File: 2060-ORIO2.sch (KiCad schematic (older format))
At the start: 195 parts, among them J11 RaspberryPI-B+header, J12 Conn_01x04, J13 Conn_01x08, J14 Conn_01x02, J15 Conn_01x08, J16 Conn_01x10, J17 Conn_01x10, J18 Conn_01x10, J19 Conn_01x10, J20 Conn_01x09, J21 Conn_01x08, J22 Conn_01x08, J23 Conn_01x08, J24 Conn_01x08, J25 Conn_01x08, J26 Conn_01x08, J27 Conn_01x02, J28 Conn_01x16, J29 Conn_01x16, J30 Conn_01x16, J31 Conn_01x08, J32 Conn_01x08, J33 Conn_01x08, J34 Conn_01x08, J35 TBL001-500-02GY-2GY, Q11 ULN2803ADWR, Q12 BCV27, SW11 SW_DIP_x08, U11 ICE40HX4K-TQ144, U12 SN74LVC4245AN, U13 SN74LVC4245AN, U14 SN74LVC4245AN, U15 TPS563231, U16 MCP3008, U17 AZ1117CH-3.3TRG1, U18 AZ1117CH-3.3TRG1, U19 AZ1117CH-1.2, U20 TPS563231, U21 SN74LVC4245AN, U22 SN74LVC4245AN, U23 SN74LVC4245AN, U24 SN74LVC4245AN, U25 TPS563231, U26 AP3012, Y11 XLH536025_000000I

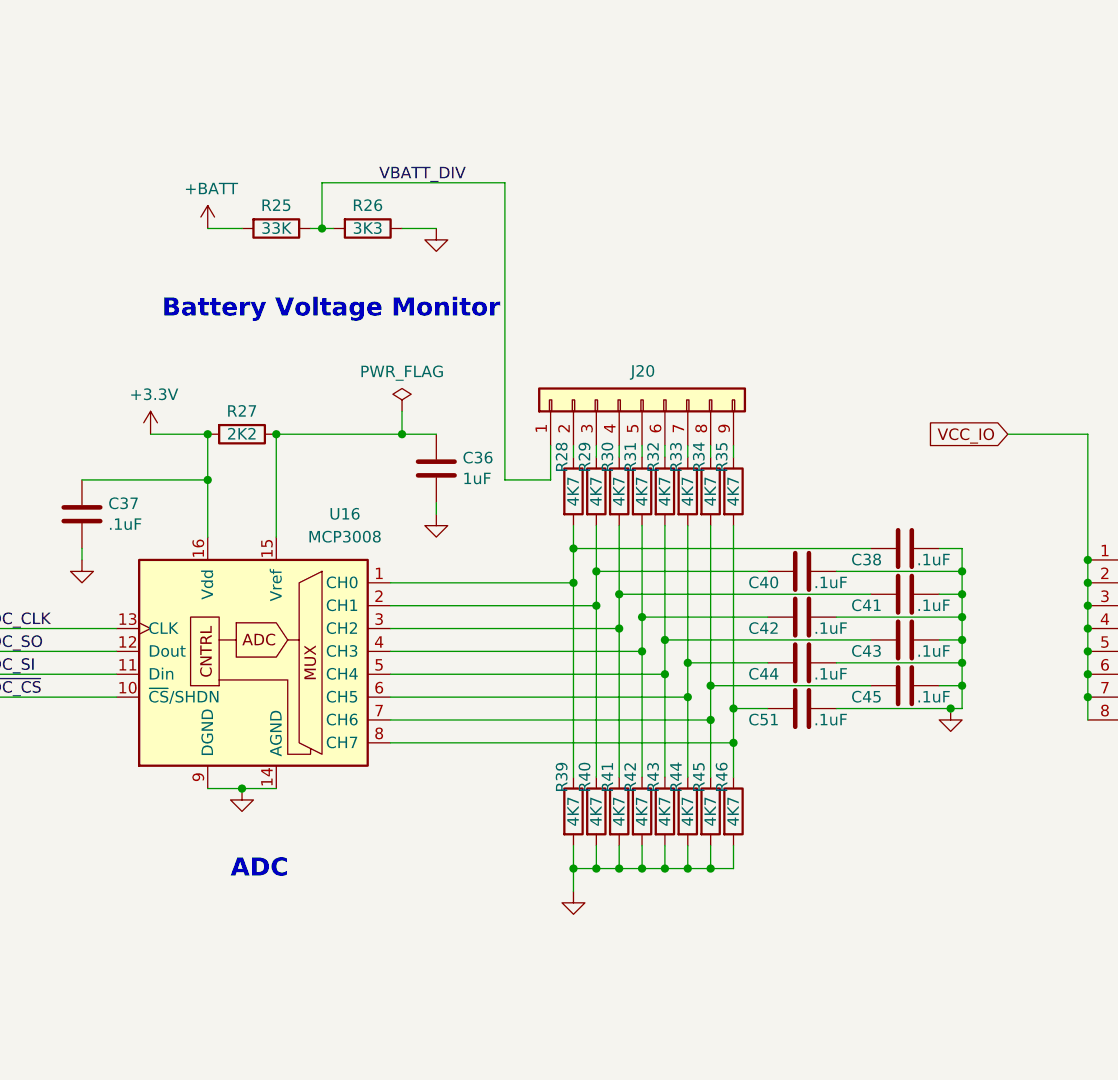
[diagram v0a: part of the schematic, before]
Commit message: Change ADC ref voltage resistor to 100 ohms.
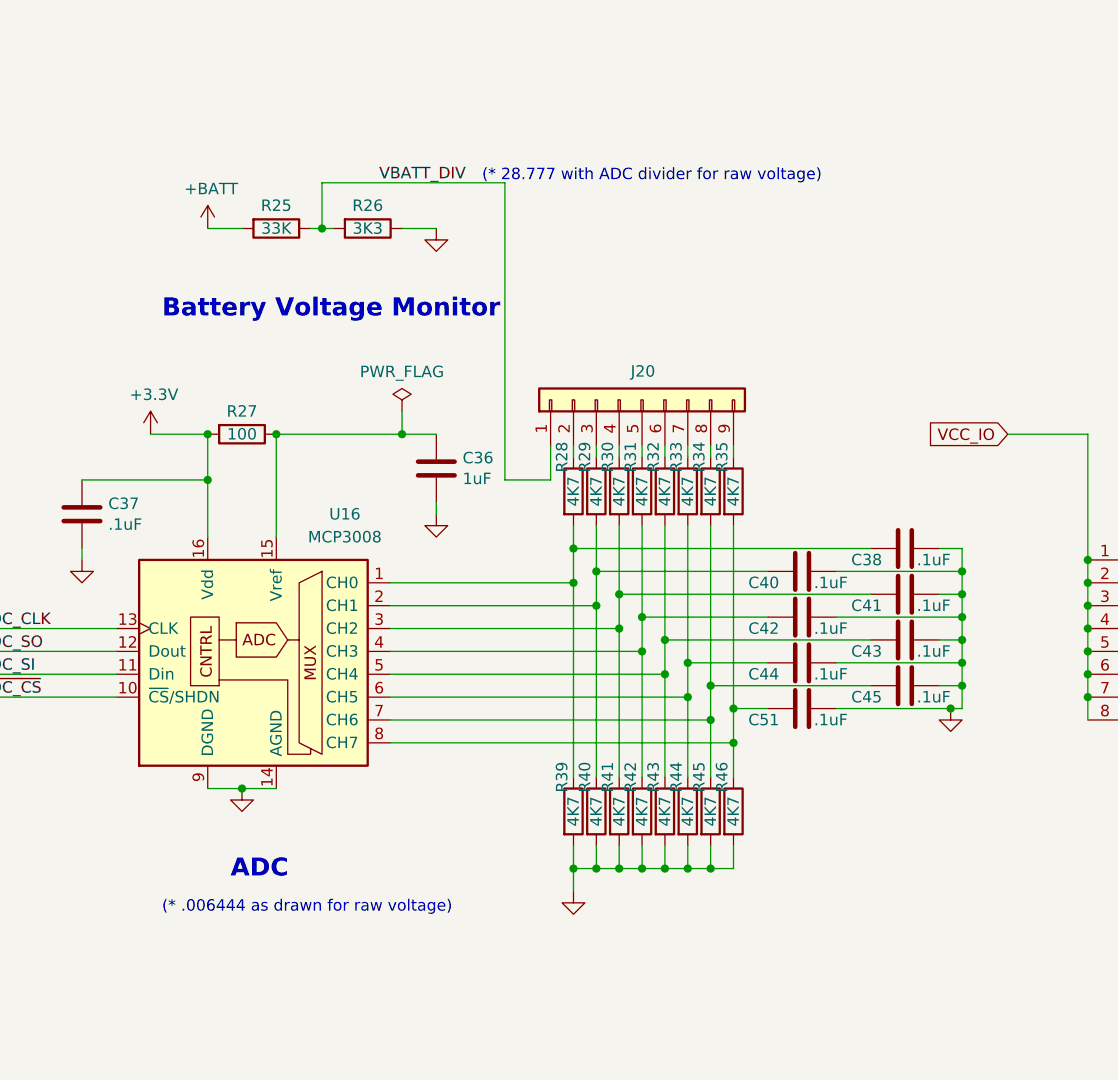
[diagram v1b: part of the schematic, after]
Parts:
- R27: value 2K2 -> 100; Description RES SMD 2.2K OHM 1% 1/10W 0603 -> RES SMD 100 OHM 1% 1/10W 0603; Digi-Key_PN 311-2.20KHRCT-ND -> 311-100HRCT-ND; MPN RC0603FR-072K2L -> RC0603FR-07100RL
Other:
- note added: "(* .006444 as drawn for raw voltage)"
- note added: "(* 28.777 with ADC divider for raw voltage)"
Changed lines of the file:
@@
 AR Path="/5ECC13DB/63C02E3E" Ref="R?"  Part="1"
 F 0 "R27" V 16450 8650 50  0000 C CNN
-F 1 "2K2" V 16550 8650 50  0000 C CNN
+F 1 "100" V 16550 8650 50  0000 C CNN
 F 2 "Resistor_SMD:R_0603_1608Metric_Pad1.05x0.95mm_HandSolder" V 16480 8650 50  0001 C CNN
 F 3 "~" H 16550 8650 50  0001 C CNN
-F 4 "311-2.20KHRCT-ND" H 16550 8650 50  0001 C CNN "Digi-Key_PN"
-F 5 "RES SMD 2.2K OHM 1% 1/10W 0603" H 16550 8650 50  0001 C CNN "Description"
-F 6 "RC0603FR-072K2L" H 16550 8650 50  0001 C CNN "MPN"
+F 4 "311-100HRCT-ND" H 16550 8650 50  0001 C CNN "Digi-Key_PN"
+F 5 "RES SMD 100 OHM 1% 1/10W 0603" H 16550 8650 50  0001 C CNN "Description"
+F 6 "RC0603FR-07100RL" H 16550 8650 50  0001 C CNN "MPN"
 F 7 "Yageo" H 16550 8650 50  0001 C CNN "Manufacturer"
 	1    16550 8650
@@
 	0    1    -1   0
 $EndComp
+Text Notes 17600 7550 0    50   ~ 0
+(* 28.777 with ADC divider for raw voltage)
+Text Notes 16200 10750 0    50   ~ 0
+(* .006444 as drawn for raw voltage)
 $EndSCHEMATC

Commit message: Change regulators & add current limiters.
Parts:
- removed C31, C33, C35, C60, C62, C69, C71: .1uF, Capacitor_SMD:C_0603_1608Metric_Pad1.05x0.95mm_HandSolder, symbol Device:C
- removed F11: .5A, Fuse:Fuse_2920_7451Metric_Pad2.10x5.45mm_HandSolder, symbol Device:Polyfuse
- removed J27: Conn_01x02, Connector_PinHeader_2.54mm:PinHeader_1x02_P2.54mm_Vertical, symbol Connector_Generic:Conn_01x02
- removed R12, R13, R15, R16, R17, R18, R19: 33, Resistor_SMD:R_0603_1608Metric_Pad1.05x0.95mm_HandSolder, symbol Device:R
- removed U12, U13, U14, U21, U22, U23, U24: SN74LVC4245AN, Package_SO:TSSOP-24_4.4x7.8mm_P0.65mm, symbol jb-symbol:SN74LVC4245AN
- removed U15, U20, U25: TPS563231, jb-footprint:SOT-563, symbol JWlib:TPS563231
- added C80, C81, C84, C85: 22uF, Capacitor_SMD:C_0805_2012Metric_Pad1.15x1.40mm_HandSolder, symbol Device:C
- added C82, C83: .001uF, Capacitor_SMD:C_0603_1608Metric_Pad1.05x0.95mm_HandSolder, symbol Device:C
- added Q91, Q92, Q93, Q94: BCV27, Package_TO_SOT_SMD:SOT-23, symbol Device:Q_NPN_Darlington_BEC
- added R55, R56, R57: x, Resistor_SMD:R_0603_1608Metric_Pad1.05x0.95mm_HandSolder, symbol Device:R
- added R91, R93: 10K, Resistor_SMD:R_0603_1608Metric_Pad1.05x0.95mm_HandSolder, symbol Device:R
- added R92, R94: 1.2, Resistor_SMD:R_1210_3225Metric_Pad1.42x2.65mm_HandSolder, symbol Device:R
- added RN14: 33, Resistor_SMD:R_Array_Convex_8x0602, symbol Device:R_Pack08
- added SW1: SW_DIP_x01, Button_Switch_THT:SW_DIP_SPSTx01_Slide_6.7x4.1mm_W7.62mm_P2.54mm_LowProfile, symbol Switch:SW_DIP_x01
- added U1, U15, U20: AOZ2151TQI-19, jb-footprint:AOZ2151TQI-19, symbol jb-symbol:AOZ2151TQI-19
- added U12, U13, U14, U21, U22, U23, U24: ‎74LVT245B, Package_SO:TSSOP-20_4.4x6.5mm_P0.65mm, symbol jb-symbol:‎74LVT245B
- C46, C67: value .1uF -> 4.7uF; Description CAP CER 0.1UF 25V X5R 0603 -> (none); Digi-Key_PN 445-6854-1-ND -> (none); MPN C1608X5R1E104K -> (none); Manufacturer TDK Corporation -> (none)
- C47: value 10uF -> 22uF; Description CAP CER 10UF 25V X5R 0805 -> (none); Digi-Key_PN 587-2985-1-ND -> (none); MPN TMK212BBJ106KG-T -> (none); Manufacturer Taiyo Yuden -> (none)
- C50, C58: value .1uF -> 22uF; footprint Capacitor_SMD:C_0603_1608Metric_Pad1.05x0.95mm_HandSolder -> Capacitor_SMD:C_0805_2012Metric_Pad1.15x1.40mm_HandSolder; Description CAP CER 0.1UF 25V X5R 0603 -> CAP CER 22UF 10V X5R 0805; Digi-Key_PN 445-6854-1-ND -> 490-10746-1-ND; MPN C1608X5R1E104K -> GRM21BR61A226ME44L; Manufacturer TDK Corporation -> Murata Electronics
- C63, C77: value .1uF -> 22uF; footprint Capacitor_SMD:C_0603_1608Metric_Pad1.05x0.95mm_HandSolder -> Capacitor_SMD:C_0805_2012Metric_Pad1.15x1.40mm_HandSolder; Description CAP CER 0.1UF 25V X5R 0603 -> (none); Digi-Key_PN 445-6854-1-ND -> (none); MPN C1608X5R1E104K -> (none); Manufacturer TDK Corporation -> (none)
- C64: value 10uF -> .1uF; footprint Capacitor_SMD:C_0805_2012Metric_Pad1.15x1.40mm_HandSolder -> Capacitor_SMD:C_0603_1608Metric_Pad1.05x0.95mm_HandSolder; Description CAP CER 10UF 25V X5R 0805 -> CAP CER 0.1UF 25V X5R 0603; Digi-Key_PN 587-2985-1-ND -> 445-6854-1-ND; MPN TMK212BBJ106KG-T -> C1608X5R1E104K; Manufacturer Taiyo Yuden -> TDK Corporation
- C73: value .1uF -> .001uF; Description CAP CER 0.1UF 25V X5R 0603 -> (none); Digi-Key_PN 445-6854-1-ND -> (none); MPN C1608X5R1E104K -> (none); Manufacturer TDK Corporation -> (none)
- C74: value 10uF -> 4.7uF; footprint Capacitor_SMD:C_0805_2012Metric_Pad1.15x1.40mm_HandSolder -> Capacitor_SMD:C_0603_1608Metric_Pad1.05x0.95mm_HandSolder; Description CAP CER 10UF 25V X5R 0805 -> (none); Digi-Key_PN 587-2985-1-ND -> (none); MPN TMK212BBJ106KG-T -> (none); Manufacturer Taiyo Yuden -> (none)
- L11, L12, L13: value 4.7uH -> 2.2uH; footprint Inductor_SMD:L_Bourns_SRN6045TA -> Inductor_SMD:L_Taiyo-Yuden_MD-4040; Description FIXED IND 4.7UH 4.5A 26 MOHM SMD -> (none); Digi-Key_PN SRN6045TA-4R7MCT-ND -> (none); MPN SRN6045TA-4R7M -> (none); Manufacturer Bourns Inc. -> (none)
- R36: value 45K3 -> x; Description RES 45.3K OHM 1% 1/10W 0603 -> (none); Digi-Key_PN RMCF0603FT45K3CT-ND -> (none); MPN RMCF0603FT45K3 -> (none); Manufacturer Stackpole Electronics Inc -> (none)
- R37, R48, R50: value 10K -> x; Description RES SMD 10K OHM 1% 1/10W 0603 -> (none); Digi-Key_PN 311-10.0KHRCT-ND -> (none); MPN RC0603FR-0710KL -> (none); Manufacturer Yageo -> (none)
- R38: value 16K2 -> x
- R47: value 73K2 -> x; Description RES SMD 73.2K OHM 1% 1/10W 0603 -> (none); Digi-Key_PN 311-73.2KHRCT-ND -> (none); MPN RC0603FR-0773K2L -> (none); Manufacturer Yageo -> (none)
- R49: value 90K -> x; Description RES 90.9K OHM 1% 1/10W 0603 -> (none); Digi-Key_PN RMCF0603FT90K9CT-ND -> (none); MPN RMCF0603FT90K9 -> (none); Manufacturer Stackpole Electronics Inc -> (none)
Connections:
- net labels added: VB_RSL, VB_RSOL
- net labels removed: VCC_SOL_12
- wire segments 1187 -> 1176
- no-connect marks 37 -> 42
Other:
- note added: ".5 Watt"
- note added: "24V @ 500mA Boost Regulator"
- note added: "500ma Current Limiter"
- note added: "5V Tolerant Quadrature Input"
- note added: "ON = 5V\nOFF = 3.3V"
- note added: "PWM output"
- note removed: "24V @ 500mA"
- note removed: "PWM w/output level shifter"
- note removed: "Quadrature VCC_IO input level shifter"
- note removed: "Shunt J35 for 5V.\nRemove for 3.3V."
- moved on the sheet: C16, C17, C18, C19, C20, C21, C22, C23, C24, C25, C26, C27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

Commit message: Change +BATT voltage divider to /6.
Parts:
- removed R26: 3K3, Resistor_SMD:R_0603_1608Metric_Pad1.05x0.95mm_HandSolder, symbol Device:R
- R25: value 33K -> 18K8
- R36: value x -> 3K4
- R37, R48, R50: value x -> 1K6
- R38: value x -> 5K
- R47: value x -> 8K4
- R49: value x -> 10K4
- R55, R56, R57: value x -> 0
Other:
- note added: "(* 6V with ADC divider for raw voltage)"
- note added: "ON = 3.3V\nOFF = 5V"
- note removed: "(* 28.777 with ADC divider for raw voltage)"
- note removed: "ON = 5V\nOFF = 3.3V"
- moved on the sheet: C47, R25, R36, R38, SW1

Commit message: Version 2.1 As ordered from JLCPCB.
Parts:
- C46, C67, C74: Description (none) -> CAP CER 4.7UF 10V X5R 0603; Digi-Key_PN (none) -> 1276-1044-1-ND; MPN (none) -> CL10A475KP8NNNC; Manufacturer (none) -> Samsung Electro-Mechanics
- C47, C63, C77: Description (none) -> CAP CER 22UF 25V X5R 0805; Digi-Key_PN (none) -> 490-14661-1-ND; MPN (none) -> GRM21BR61E226ME44K; Manufacturer (none) -> Murata Electronics
- C73, C82, C83: Description (none) -> CAP CER 1000PF 50V X7R 0603; Digi-Key_PN (none) -> 478-1215-1-ND; MPN (none) -> 06035C102KAT2A; Manufacturer (none) -> AVX Corporation
- H11, H12, H13, H14, H15, H16, H17, H18: Description (none) -> x; Digi-Key_PN (none) -> x; MPN (none) -> x
- J11, J12, J16, J17, J18, J19: Description (none) -> x; Digi-Key_PN (none) -> x; MPN (none) -> x; Manufacturer (none) -> x
- L11, L12, L13: Description (none) -> FIXED IND 2.2UH 4.3A 48 MOHM SMD; Digi-Key_PN (none) -> 553-3290-1-ND; MPN (none) -> PA4332.222NLT; Manufacturer (none) -> Pulse Electronics Power
- R25: Description RES SMD 33K OHM 1% 1/10W 0603 -> RES SMD 18K OHM 1% 1/10W 0603; Digi-Key_PN 311-33.0KHRCT-ND -> 311-18.0KHRCT-ND; MPN RC0603FR-0733KL -> RC0603FR-0718KL
- R36: Description (none) -> RES 3.4K OHM 1% 1/10W 0603; Digi-Key_PN (none) -> RMCF0603FT3K40CT-ND; MPN (none) -> RMCF0603FT3K40; Manufacturer (none) -> Stackpole Electronics Inc
- R37, R48, R50: Description (none) -> RES 1.6K OHM 1% 1/10W 0603; Digi-Key_PN (none) -> RMCF0603FT1K60CT-ND; MPN (none) -> RMCF0603FT1K60; Manufacturer (none) -> Stackpole Electronics Inc
- R38: Description RES 16.2K OHM 1% 1/10W 0603 -> RES SMD 5.1K OHM 1% 1/10W 0603; Digi-Key_PN RMCF0603FT16K2CT-ND -> CR0603-FX-5101ELFCT-ND; MPN RMCF0603FT16K2 -> CR0603-FX-5101ELF; Manufacturer Stackpole Electronics Inc -> Bourns Inc.
- R47: Description (none) -> RES 8.45K OHM 1% 1/10W 0603; Digi-Key_PN (none) -> RMCF0603FT8K45CT-ND; MPN (none) -> RMCF0603FT8K45; Manufacturer (none) -> Stackpole Electronics Inc
- R49: Description (none) -> RES 10.5K OHM 1% 1/10W 0603; Digi-Key_PN (none) -> RMCF0603FT10K5CT-ND; MPN (none) -> RMCF0603FT10K5; Manufacturer (none) -> Stackpole Electronics Inc
- R91, R93: Description (none) -> RES SMD 10K OHM 1% 1/10W 0603; Digi-Key_PN (none) -> 311-10.0KHRT-ND; MPN (none) -> RC0603FR-0710KL; Manufacturer (none) -> Yageo
- R92, R94: Description (none) -> RES 1.21 OHM 1% 1/2W 1210; Digi-Key_PN (none) -> RMCF1210FT1R21CT-ND; MPN (none) -> RMCF1210FT1R21; Manufacturer (none) -> Stackpole Electronics Inc
- SW1: Description (none) -> DIP SWITCH, SPST, 2.54 PITCH, RA; Digi-Key_PN (none) -> 2223-DS04-254-1L-01BK-ND; MPN (none) -> DS04-254-1L-01BK; Manufacturer (none) -> CUI Devices
- U1, U15, U20: Description (none) -> POWER IC EZBUCK; Digi-Key_PN (none) -> 785-1868-1-ND; MPN (none) -> AOZ2151TQI-19; Manufacturer (none) -> Alpha & Omega Semiconductor Inc.
- U12, U13, U14, U21, U22, U23, U24: Description (none) -> IC TXRX NON-INVERT 3.6V 20TSSOP; Digi-Key_PN (none) -> 1727-6005-1-ND; MPN (none) -> 74LVT245BPW,118; Manufacturer (none) -> Nexperia USA Inc.
